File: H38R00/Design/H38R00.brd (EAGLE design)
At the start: 34.6 x 60 mm, 72 parts, among them P1 HEXABIT_17.32_X2_POWER_ONLY, U1 LM5160DNT, U2 TPS65130RGERT

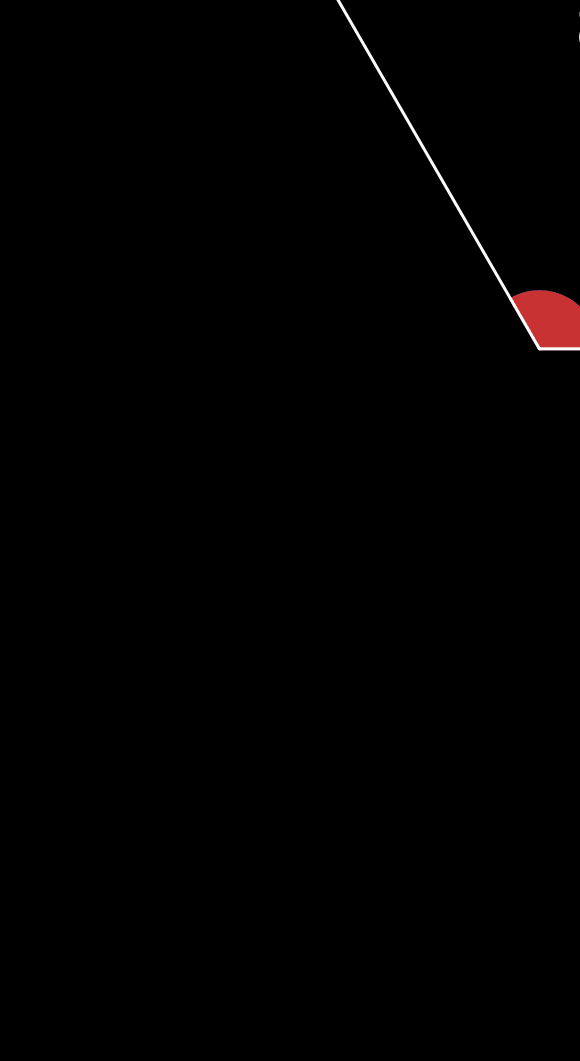
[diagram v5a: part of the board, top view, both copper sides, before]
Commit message: added 3.3V LDO on 5V output
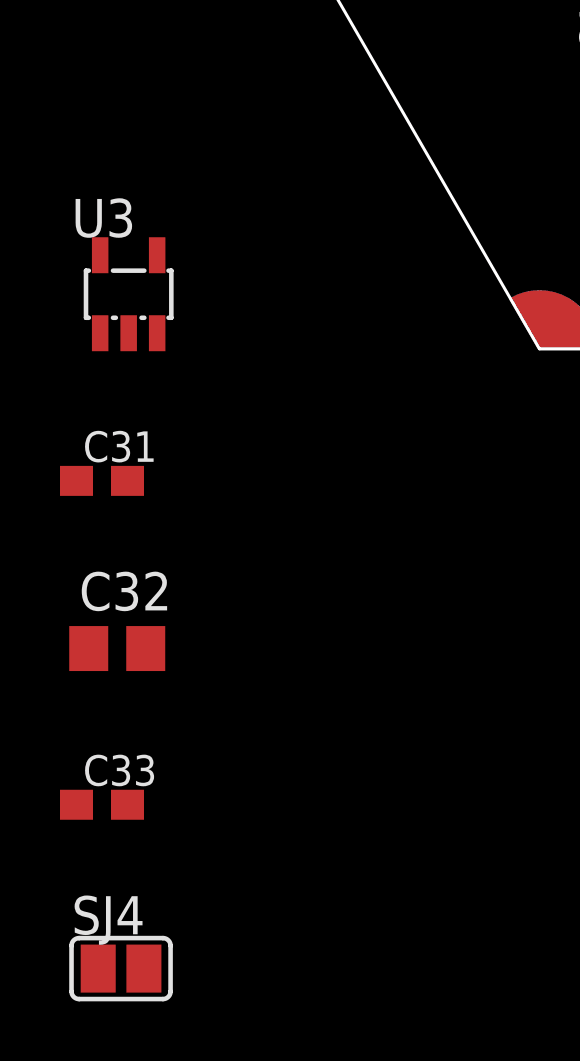
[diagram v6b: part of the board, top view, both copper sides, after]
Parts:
- added C31: 10nF, Hexabitz:C-0603
- added C32: 10uF, Hexabitz:C-0805
- added C33: 100nF, Hexabitz:C-0603
- added SJ4: (no value), jumper:SJ
- added U3: TPS76433DBVT, Hexabitz:SOT25
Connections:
- removed net GND1: P1.PAD_PD11
- removed net GND10: P1.PAD_PD20
- removed net GND2: P1.PAD_PD12
- removed net GND9: P1.PAD_PD19
- removed net VDD1: P1.PAD_PU11
- removed net VDD10: P1.PAD_PU20
- removed net VDD2: P1.PAD_PU12
- removed net VDD9: P1.PAD_PU19
- new net +3V3: C32.1, C33.1, P1.PAD_PU11, P1.PAD_PU12, P1.PAD_PU19, P1.PAD_PU20, U3.5
- new net N$35: C31.1, U3.4
- new net N$36: SJ4.1, U3.1, U3.3
- net +5V: now also SJ4.2
- net AGND: now also C31.2, C32.2, C33.2, P1.PAD_PD11, P1.PAD_PD12, P1.PAD_PD19, P1.PAD_PD20, U3.2
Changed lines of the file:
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@@
 <attribute name="VALUE" x="47.284553125" y="70.164821875" size="1.016" layer="27" rot="R210"/>
+</element>
+<element name="U3" library="Hexabitz" package="SOT25" package3d_urn="urn:adsk.eagle:package:30378/1" value="TPS76433DBVT" x="10.668" y="21.336" smashed="yes">
+<attribute name="MFN" value="Texas Instruments" x="10.668" y="21.336" size="1.778" layer="27" display="off"/>
+<attribute name="MPN" value="TPS76433DBVT" x="10.668" y="21.336" size="1.778" layer="27" display="off"/>
+<attribute name="NAME" x="8.763" y="23.241" size="1.27" layer="25"/>
+<attribute name="OCTOPART_URL" value="https://octopart.com/tps76433dbvt-texas+instruments-69873?r=sp&amp;s=0aHKKhMLSUCTmmqJkhwwIQ" x="10.668" y="21.336" size="1.778" layer="27" display="off"/>
+<attribute name="VALUE" x="8.763" y="17.907" size="1.27" layer="27"/>
+</element>
+<element name="C31" library="Hexabitz" package="C-0603" value="10nF" x="9.779" y="15.113" smashed="yes">
+<attribute name="CAPACITANCE" value="10nF" x="9.779" y="15.113" size="1.778" layer="27" display="off"/>
+<attribute name="MFN" value="Würth Elektronik" x="9.779" y="15.113" size="1.778" layer="27" display="off"/>
+<attribute name="MPN" value="885012206040" x="9.779" y="15.113" size="1.778" layer="27" display="off"/>
+<attribute name="NAME" x="9.144" y="15.748" size="1.016" layer="25"/>
+<attribute name="OCTOPART_URL" value="https://octopart.com/885012206040-w%C3%BCrth+elektronik-53914749?r=sp&amp;s=G3_ezLbARM2-FohtMFECqg" x="9.779" y="15.113" size="1.778" layer="27" display="off"/>
+<attribute name="TOLERANCE" value="10%" x="9.779" y="15.113" size="1.778" layer="27" display="off"/>
+<attribute name="VALUE" x="9.144" y="13.208" size="1.016" layer="27"/>
+<attribute name="VOLTAGE_RATING" value="16V" x="9.779" y="15.113" size="1.778" layer="27" display="off"/>
+</element>
+<element name="C32" library="Hexabitz" package="C-0805" value="10uF" x="10.287" y="9.525" smashed="yes">
+<attribute name="CAPACITANCE" value="10uF" x="10.287" y="9.525" size="1.778" layer="27" display="off"/>
+<attribute name="MFN" value="Murata" x="10.287" y="9.525" size="1.778" layer="27" display="off"/>
+<attribute name="MPN" value="GRM21BC71E106KE11L" x="10.287" y="9.525" size="1.778" layer="27" display="off"/>
+<attribute name="NAME" x="9.017" y="10.795" size="1.27" layer="25"/>
+<attribute name="OCTOPAR_URL" value="https://octopart.com/grm21bc71e106ke11l-murata-51454492?r=sp&amp;s=2Vde2RpCRyqy5YYMvYke3Q" x="10.287" y="9.525" size="1.778" layer="27" display="off"/>
+<attribute name="TOLERANCE" value="10%" x="10.287" y="9.525" size="1.778" layer="27" display="off"/>
+<attribute name="VALUE" x="9.017" y="6.985" size="1.27" layer="27"/>
+<attribute name="VOLTAGE_RATING" value="25V" x="10.287" y="9.525" size="1.778" layer="27" display="off"/>
+</element>
+<element name="C33" library="Hexabitz" package="C-0603" value="100nF" x="9.779" y="4.318" smashed="yes">
+<attribute name="CAPACITANCE" value="100nF" x="9.779" y="4.318" size="1.778" layer="27" display="off"/>
+<attribute name="MFN" value="TDK" x="9.779" y="4.318" size="1.778" layer="27" display="off"/>
+<attribute name="MPN" value="C1608X7R1H104K" x="9.779" y="4.318" size="1.778" layer="27" display="off"/>
+<attribute name="NAME" x="9.144" y="4.953" size="1.016" layer="25"/>
+<attribute name="OCTOPART_URL" value="https://octopart.com/c1608x7r1h104k080aa-tdk-25947665?r=sp&amp;s=vJ3_28x5RGekN18MBHqpKw" x="9.779" y="4.318" size="1.778" layer="27" display="off"/>
+<attribute name="TOLERANCE" value="10%" x="9.779" y="4.318" size="1.778" layer="27" display="off"/>
+<attribute name="VALUE" x="9.144" y="2.413" size="1.016" layer="27"/>
+<attribute name="VOLTAGE_RATING" value="50V" x="9.779" y="4.318" size="1.778" layer="27" display="off"/>
+</element>
+<element name="SJ4" library="jumper" library_urn="urn:adsk.eagle:library:252" package="SJ" package3d_urn="urn:adsk.eagle:package:15471/1" value="" x="10.414" y="-1.143" smashed="yes">
+<attribute name="NAME" x="8.763" y="0" size="1.27" layer="25" ratio="10"/>
+<attribute name="VALUE" x="10.8141" y="-1.143" size="0.02" layer="27"/>
 </element>
 </elements>
@@
 <contactref element="D4" pad="C"/>
 <contactref element="D6" pad="A"/>
+<contactref element="U3" pad="2"/>
+<contactref element="C31" pad="2"/>
+<contactref element="C32" pad="2"/>
+<contactref element="C33" pad="2"/>
+<contactref element="P1" pad="PAD_PD11"/>
+<contactref element="P1" pad="PAD_PD12"/>
+<contactref element="P1" pad="PAD_PD19"/>
+<contactref element="P1" pad="PAD_PD20"/>
+<wire x1="41.710396875" y1="71.82354375" x2="41.28" y2="78.8227375" width="0" layer="19" extent="16-16"/>
 <wire x1="39.751" y1="68.795" x2="41.710396875" y2="71.82354375" width="0" layer="19" extent="16-16"/>
 <wire x1="37.338" y1="68.795" x2="39.751" y2="68.795" width="0" layer="19" extent="16-16"/>
@@
 <wire x1="21.75" y1="63.058275" x2="26.587" y2="66.39511875" width="0" layer="19" extent="1-16"/>
 <wire x1="19.718" y1="64.201275" x2="21.75" y2="63.058275" width="0" layer="19" extent="16-16"/>
+<wire x1="16.5" y1="64.516" x2="19.718" y2="64.201275" width="0" layer="19" extent="16-16"/>
 <wire x1="19.044" y1="67.57851875" x2="19.718" y2="64.201275" width="0" layer="19" extent="1-16"/>
 <wire x1="44.036" y1="62.931275" x2="37.934" y2="62.611" width="0" layer="19" extent="1-16"/>
 <wire x1="46.195" y1="64.201275" x2="44.036" y2="62.931275" width="0" layer="19" extent="16-16"/>
 <wire x1="47.365" y1="66.025478125" x2="46.195" y2="64.201275" width="0" layer="19" extent="1-16"/>
+<wire x1="49.54" y1="64.516" x2="47.365" y2="66.025478125" width="0" layer="19" extent="1-16"/>
 <wire x1="42.037" y1="57.062" x2="44.036" y2="62.931275" width="0" layer="19" extent="1-16"/>
-<wire x1="28.194" y1="78.22" x2="34.77" y2="75.719" width="0" layer="19" extent="1-1"/>
+<wire x1="24.760003125" y1="78.8227375" x2="24.3296" y2="71.82354375" width="0" layer="19" extent="16-16"/>
+<wire x1="28.194" y1="78.22" x2="24.760003125" y2="78.8227375" width="0" layer="19" extent="1-16"/>
 <wire x1="38.227" y1="50.903" x2="42.037" y2="57.062" width="0" layer="19" extent="1-1"/>
-</signal>
-<signal name="GND10">
-<contactref element="P1" pad="PAD_PD20"/>
-</signal>
-<signal name="GND9">
-<contactref element="P1" pad="PAD_PD19"/>
+<wire x1="10.668" y1="20.036" x2="28.93599375" y2="52.217003125" width="0" layer="19" extent="1-1"/>
+<wire x1="10.629" y1="15.113" x2="10.668" y2="20.036" width="0" layer="19" extent="1-1"/>
+<wire x1="11.237" y1="9.525" x2="10.629" y2="15.113" width="0" layer="19" extent="1-1"/>
+<wire x1="10.629" y1="4.318" x2="11.237" y2="9.525" width="0" layer="19" extent="1-1"/>
 </signal>
 <signal name="GND8">
@@
 <contactref element="P1" pad="PAD_PD13"/>
 </signal>
-<signal name="GND1">
-<contactref element="P1" pad="PAD_PD11"/>
-</signal>
-<signal name="GND2">
-<contactref element="P1" pad="PAD_PD12"/>
-</signal>
-<signal name="VDD1">
-<contactref element="P1" pad="PAD_PU11"/>
-</signal>
 <signal name="VDD5">
 <contactref element="P1" pad="PAD_PU15"/>
@@
 <contactref element="P1" pad="PAD_PU17"/>
 </signal>
-<signal name="VDD9">
-<contactref element="P1" pad="PAD_PU19"/>
-</signal>
-<signal name="VDD10">
-<contactref element="P1" pad="PAD_PU20"/>
-</signal>
 <signal name="VDD8">
 <contactref element="P1" pad="PAD_PU18"/>
@@
 <signal name="VDD3">
 <contactref element="P1" pad="PAD_PU13"/>
-</signal>
-<signal name="VDD2">
-<contactref element="P1" pad="PAD_PU12"/>
 </signal>
 <signal name="N$1">
@@
 <contactref element="SJ3" pad="1"/>
 <contactref element="FB1" pad="1"/>
+<contactref element="SJ4" pad="2"/>
 <wire x1="32.043" y1="70.739" x2="31.27" y2="75.719" width="0" layer="19" extent="16-16"/>
 <wire x1="31.943" y1="68.453" x2="32.043" y2="70.739" width="0" layer="19" extent="16-16"/>
@@
 <wire x1="33.694" y1="59.436" x2="31.943" y2="68.453" width="0" layer="19" extent="1-16"/>
 <wire x1="33.694" y1="57.15" x2="33.694" y2="59.436" width="0" layer="19" extent="1-1"/>
+<wire x1="11.176" y1="-1.143" x2="33.694" y2="57.15" width="0" layer="19" extent="1-1"/>
 </signal>
 <signal name="+15V">
@@
 <wire x1="46.45611875" y1="64.306" x2="46.615" y2="67.32451875" width="0" layer="19" extent="1-1"/>
 </signal>
+<signal name="+3V3">
+<contactref element="U3" pad="5"/>
+<contactref element="C32" pad="1"/>
+<contactref element="C33" pad="1"/>
+<contactref element="P1" pad="PAD_PU12"/>
+<contactref element="P1" pad="PAD_PU11"/>
+<contactref element="P1" pad="PAD_PU20"/>
+<contactref element="P1" pad="PAD_PU19"/>
+<wire x1="49.54" y1="64.516" x2="41.28" y2="78.8227375" width="0" layer="19" extent="1-1"/>
+<wire x1="24.760003125" y1="78.8227375" x2="41.28" y2="78.8227375" width="0" layer="19" extent="1-1"/>
+<wire x1="16.5" y1="64.516" x2="24.760003125" y2="78.8227375" width="0" layer="19" extent="1-1"/>
+<wire x1="9.718" y1="22.636" x2="16.5" y2="64.516" width="0" layer="19" extent="1-1"/>
+<wire x1="9.337" y1="9.525" x2="9.718" y2="22.636" width="0" layer="19" extent="1-1"/>
+<wire x1="8.929" y1="4.318" x2="9.337" y2="9.525" width="0" layer="19" extent="1-1"/>
+</signal>
+<signal name="N$35">
+<contactref element="U3" pad="4"/>
+<contactref element="C31" pad="1"/>
+<wire x1="8.929" y1="15.113" x2="11.618" y2="22.636" width="0" layer="19" extent="1-1"/>
+</signal>
+<signal name="N$36">
+<contactref element="U3" pad="3"/>
+<contactref element="U3" pad="1"/>
+<contactref element="SJ4" pad="1"/>
+<wire x1="9.718" y1="20.036" x2="11.618" y2="20.036" width="0" layer="19" extent="1-1"/>
+<wire x1="9.652" y1="-1.143" x2="9.718" y2="20.036" width="0" layer="19" extent="1-1"/>
+</signal>
 </signals>

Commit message: Arranged most silkscreen Added labels
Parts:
- removed SJ1, SJ4: (no value), jumper:SJ
- added J+15, J3V3: (no value), jumper:SJ
- moved C33 63.4 mm to (42.3, 58.8), flipped to the bottom, turned to 90 degrees
- moved C32 54.8 mm to (39.1, 56.1), flipped to the bottom
- moved C31 54.8 mm to (39.0, 61.5), flipped to the bottom
- moved U3 47.1 mm to (39.0, 58.9), flipped to the bottom, turned to 90 degrees
- moved D1 0.99 mm to (25.8, 59.4), turned to 120 degrees
- moved C13 0.13 mm to (27.1, 62.7)
- moved C20 0.13 mm to (38.2, 49.5)
- moved R7 0.13 mm to (29.6, 62.7)
- renumbered SJ2 to J-15, SJ3 to J5
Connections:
- net +15V: now also J+15.1; no longer SJ1.1
- net +5V: now also J3V3.2; no longer SJ4.2
- net N$31: now also J+15.2; no longer SJ1.2
- net N$36: now also J3V3.1; no longer SJ4.1
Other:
- board text added: "+15V"
- board text added: "+5V"
- board text added: "-15V"
- board text added: "12V .. 36V"
- board text added: "IGND"

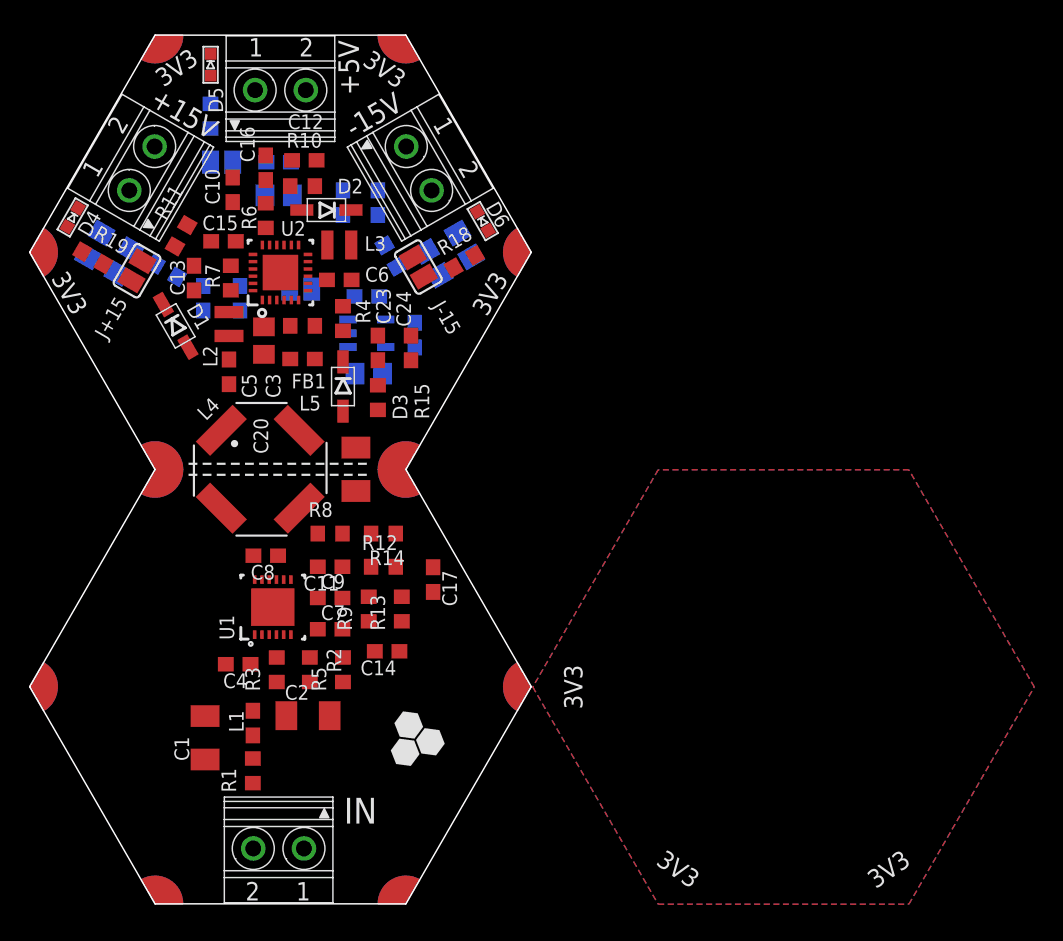
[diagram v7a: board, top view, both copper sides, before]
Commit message: Finished arranging silkscreen Added polygons and isolation barrier
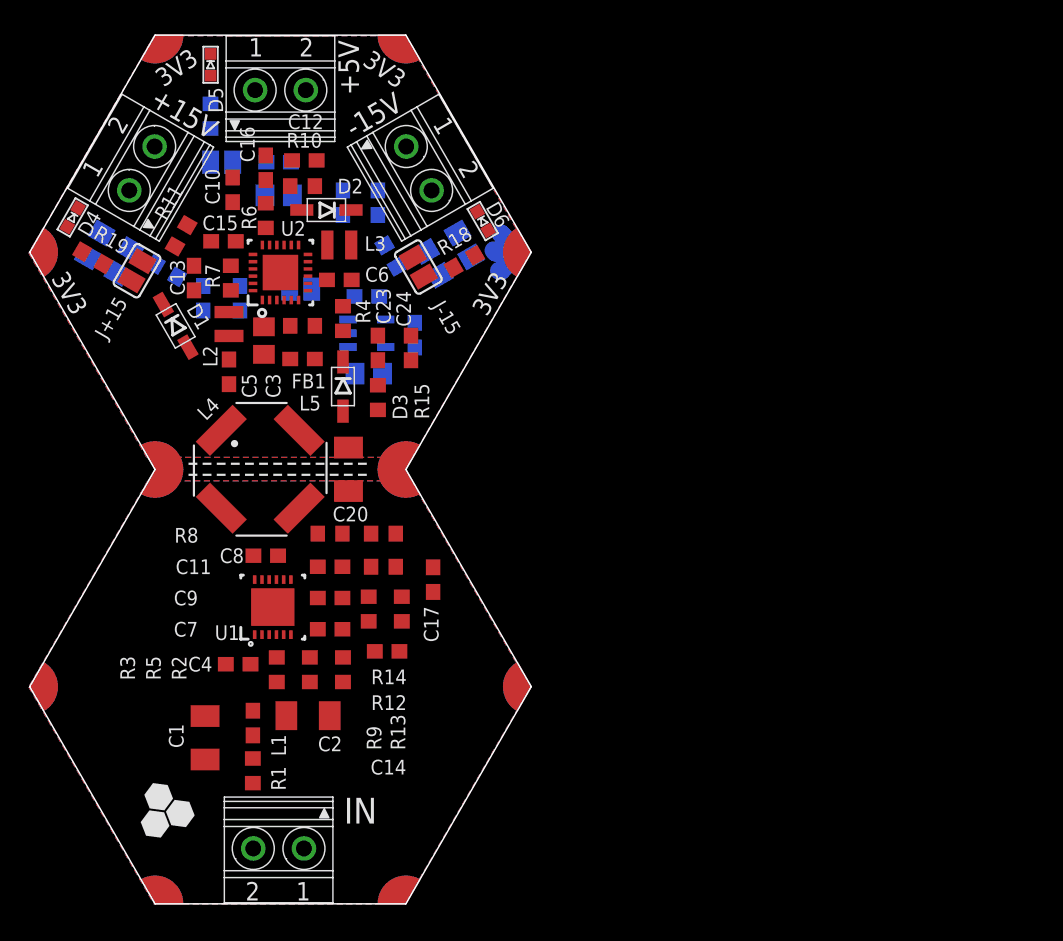
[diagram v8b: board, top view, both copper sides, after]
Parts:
- moved C20 0.51 mm to (37.7, 49.5)
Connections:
- net AGND renamed IGND
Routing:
- net IGND: track 0.00 -> 5.58 mm
- added copper zone on layer 1, net GND
- added copper zone on layer 1, net IGND
- added copper zone on layer 16, net IGND
- removed copper zone on layer 1, net VDD
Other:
- board text added: "BARRIER"
- board text added: "ISOLATION"
- board text removed: "B"
- board text removed: "C"
- board text removed: "D"
- board text removed: "R"
